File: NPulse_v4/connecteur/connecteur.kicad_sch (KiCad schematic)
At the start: 72 parts, among them J1 Conn_01x01, J10 Conn_02x05_Odd_Even, J11 Conn_01x01, J12 Conn_01x01, J13 Conn_02x05_Odd_Even, J14 Conn_01x01, J15 Conn_01x01, J16 Conn_01x01, J17 Conn_01x01, J18 Conn_01x01, J19 Conn_01x01, J2 Conn_01x01, J20 Conn_01x01, J21 Conn_01x01, J22 Conn_01x01, J23 Conn_01x01, J25 Conn_01x01, J26 Conn_01x01, J27 Conn_01x01, J29 Conn_01x01, J3 Conn_01x01, J30 Conn_01x01, J32 Conn_02x05_Odd_Even, J34 Conn_01x01, J35 Conn_02x05_Odd_Even, J36 Conn_01x01, J37 Conn_01x01, J38 Conn_01x01, J39 Conn_01x01, J4 Conn_01x01, J40 Conn_01x01, J41 Conn_01x01, J42 Conn_01x01, J43 Conn_01x01, J44 Conn_01x01, J45 Conn_01x01, J46 Conn_01x01, J47 Conn_01x01, J48 Conn_01x01, J49 Conn_01x01, J5 Conn_01x01, J50 Conn_01x01, J51 Conn_01x01, J52 Conn_01x01, J53 Conn_01x01, J54 Conn_02x05_Odd_Even, J55 Conn_01x01, J56 Conn_01x01, J57 Conn_02x05_Odd_Even, J58 Conn_01x01, J59 Conn_01x01, J6 Conn_01x01, J60 Conn_01x01, J61 Conn_01x01, J62 Conn_01x01, J63 Conn_01x01, J64 Conn_01x01, J65 Conn_01x01, J66 Conn_01x01, J67 Conn_01x01, J68 Conn_01x01, J69 Conn_01x01, J7 Conn_01x01, J70 Conn_01x01, J71 Conn_01x01, J72 Conn_01x01, J73 Conn_01x01, J74 Conn_01x01, J75 Conn_01x01, J76 Conn_01x01, J8 Conn_01x01, J9 Conn_01x01

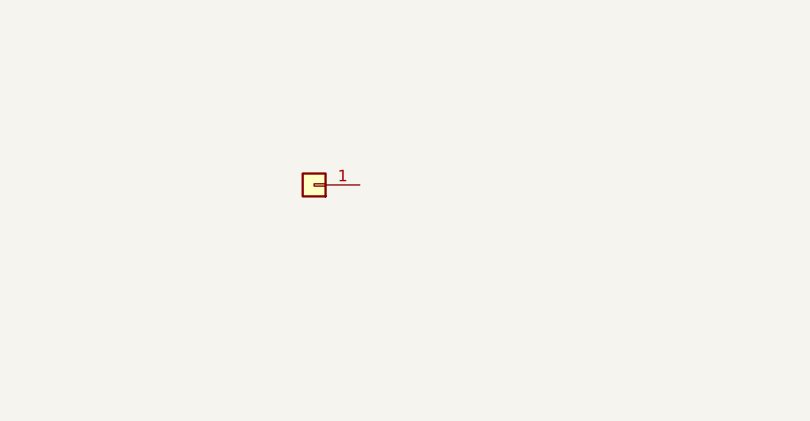
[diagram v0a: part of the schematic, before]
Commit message: Udate mounting holes positions
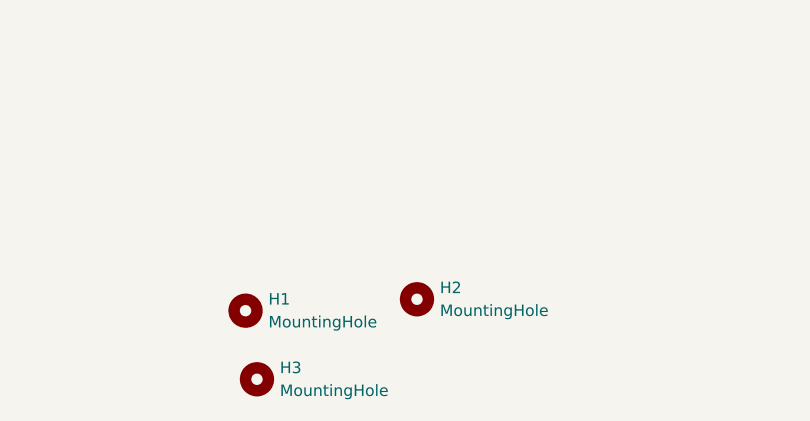
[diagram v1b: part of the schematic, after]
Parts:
- removed J71: Conn_01x01, Connector_Wire:SolderWire-0.1sqmm_1x01_D0.4mm_OD1mm, symbol Connector_Generic:Conn_01x01
- added H1, H2, H3: MountingHole, MountingHole:MountingHole_2.2mm_M2, symbol Mechanical:MountingHole
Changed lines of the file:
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@@
 (kicad_sch
-	(version 20231120)
+	(version 20250114)
 	(generator "eeschema")
-	(generator_version "8.0")
+	(generator_version "9.0")
 	(paper "A4")
 	(junction
@@
 	(label "+12V"
 		(at 179.07 72.39 90)
-		(fields_autoplaced yes)
 		(effects
 			(font
@@
 	(label "GND"
 		(at 207.01 50.8 90)
-		(fields_autoplaced yes)
 		(effects
 			(font
@@
 	(label "SCK_CON"
 		(at 181.61 50.8 90)
-		(fields_autoplaced yes)
 		(effects
 			(font
@@
 	(label "+12V"
 		(at 179.07 50.8 90)
-		(fields_autoplaced yes)
 		(effects
 			(font
@@
 	(label "MOSI_CON"
 		(at 184.15 50.8 90)
-		(fields_autoplaced yes)
 		(effects
 			(font
@@
 	(label "GND"
 		(at 204.47 50.8 90)
-		(fields_autoplaced yes)
 		(effects
 			(font
@@
 	(label "GND"
 		(at 196.85 50.8 90)
-		(fields_autoplaced yes)
 		(effects
 			(font
@@
 	(label "+5V"
 		(at 173.99 50.8 90)
-		(fields_autoplaced yes)
 		(effects
 			(font
@@
 	(label "+12V"
 		(at 176.53 72.39 90)
-		(fields_autoplaced yes)
 		(effects
 			(font
@@
 	(label "+12V"
 		(at 176.53 50.8 90)
-		(fields_autoplaced yes)
 		(effects
 			(font
@@
 	(label "MISO_CON"
 		(at 184.15 72.39 90)
-		(fields_autoplaced yes)
 		(effects
 			(font
@@
 	(label "NSS_CON"
 		(at 181.61 72.39 90)
-		(fields_autoplaced yes)
 		(effects
 			(font
@@
 	(label "GND"
 		(at 201.93 50.8 90)
-		(fields_autoplaced yes)
 		(effects
 			(font
@@
 	(label "GND"
 		(at 199.39 50.8 90)
-		(fields_autoplaced yes)
 		(effects
 			(font
@@
 	)
 	(symbol
+		(lib_id "Mechanical:MountingHole")
+		(at 134.62 167.64 0)
+		(unit 1)
+		(exclude_from_sim yes)
+		(in_bom no)
+		(on_board yes)
+		(dnp no)
+		(fields_autoplaced yes)
+		(property "Reference" "H2"
+			(at 137.16 166.3699 0)
+			(effects
+				(font
+					(size 1.27 1.27)
+				)
+				(justify left)
+			)
+		)
+		(property "Value" "MountingHole"
+			(at 137.16 168.9099 0)
+			(effects
+				(font
+					(size 1.27 1.27)
+				)
+				(justify left)
+			)
+		)
+		(property "Footprint" "MountingHole:MountingHole_2.2mm_M2"
+			(at 134.62 167.64 0)
+			(effects
+				(font
+					(size 1.27 1.27)
+				)
+				(hide yes)
+			)
+		)
+		(property "Datasheet" "~"
+			(at 134.62 167.64 0)
+			(effects
+				(font
+					(size 1.27 1.27)
+				)
+				(hide yes)
+			)
+		)
+		(property "Description" "Mounting Hole without connection"
+			(at 134.62 167.64 0)
+			(effects
+				(font
+					(size 1.27 1.27)
+				)
+				(hide yes)
+			)
+		)
+		(instances
+			(project "connecteur"
+				(path "/d1d459bc-21c9-4561-bf30-d30bab78c009"
+					(reference "H2")
+					(unit 1)
+				)
+			)
+		)
+	)
+	(symbol
 		(lib_id "power:+5V")
 		(at 196.85 96.52 0)
@@
 	)
 	(symbol
+		(lib_id "Mechanical:MountingHole")
+		(at 116.84 176.53 0)
+		(unit 1)
+		(exclude_from_sim yes)
+		(in_bom no)
+		(on_board yes)
+		(dnp no)
+		(fields_autoplaced yes)
+		(property "Reference" "H3"
+			(at 119.38 175.2599 0)
+			(effects
+				(font
+					(size 1.27 1.27)
+				)
+				(justify left)
+			)
+		)
+		(property "Value" "MountingHole"
+			(at 119.38 177.7999 0)
+			(effects
+				(font
+					(size 1.27 1.27)
+				)
+				(justify left)
+			)
+		)
+		(property "Footprint" "MountingHole:MountingHole_2.2mm_M2"
+			(at 116.84 176.53 0)
+			(effects
+				(font
+					(size 1.27 1.27)
+				)
+				(hide yes)
+			)
+		)
+		(property "Datasheet" "~"
+			(at 116.84 176.53 0)
+			(effects
+				(font
+					(size 1.27 1.27)
+				)
+				(hide yes)
+			)
+		)
+		(property "Description" "Mounting Hole without connection"
+			(at 116.84 176.53 0)
+			(effects
+				(font
+					(size 1.27 1.27)
+				)
+				(hide yes)
+			)
+		)
+		(instances
+			(project "connecteur"
+				(path "/d1d459bc-21c9-4561-bf30-d30bab78c009"
+					(reference "H3")
+					(unit 1)
+				)
+			)
+		)
+	)
+	(symbol
 		(lib_id "power:+5V")
 		(at 115.57 116.84 270)
@@
 	)
 	(symbol
+		(lib_id "Mechanical:MountingHole")
+		(at 115.57 168.91 0)
+		(unit 1)
+		(exclude_from_sim yes)
+		(in_bom no)
+		(on_board yes)
+		(dnp no)
+		(fields_autoplaced yes)
+		(property "Reference" "H1"
+			(at 118.11 167.6399 0)
+			(effects
+				(font
+					(size 1.27 1.27)
+				)
+				(justify left)
+			)
+		)
+		(property "Value" "MountingHole"
+			(at 118.11 170.1799 0)
+			(effects
+				(font
+					(size 1.27 1.27)
+				)
+				(justify left)
+			)
+		)
+		(property "Footprint" "MountingHole:MountingHole_2.2mm_M2"
+			(at 115.57 168.91 0)
+			(effects
+				(font
+					(size 1.27 1.27)
+				)
+				(hide yes)
+			)
+		)
+		(property "Datasheet" "~"
+			(at 115.57 168.91 0)
+			(effects
+				(font
+					(size 1.27 1.27)
+				)
+				(hide yes)
+			)
+		)
+		(property "Description" "Mounting Hole without connection"
+			(at 115.57 168.91 0)
+			(effects
+				(font
+					(size 1.27 1.27)
+				)
+				(hide yes)
+			)
+		)
+		(instances
+			(project ""
+				(path "/d1d459bc-21c9-4561-bf30-d30bab78c009"
+					(reference "H1")
+					(unit 1)
+				)
+			)
+		)
+	)
+	(symbol
 		(lib_id "Connector_Generic:Conn_01x01")
 		(at 242.57 73.66 0)
@@
 	(symbol
 		(lib_id "Connector_Generic:Conn_01x01")
-		(at 123.19 154.94 180)
-		(unit 1)
-		(exclude_from_sim no)
-		(in_bom yes)
-		(on_board yes)
-		(dnp no)
-		(fields_autoplaced yes)
-		(property "Reference" "J71"
-			(at 123.19 148.59 0)
-			(effects
-				(font
-					(size 1.27 1.27)
-				)
-				(hide yes)
-			)
-		)
-		(property "Value" "Conn_01x01"
-			(at 123.19 151.13 0)
-			(effects
-				(font
-					(size 1.27 1.27)
-				)
-				(hide yes)
-			)
-		)
-		(property "Footprint" "Connector_Wire:SolderWire-0.1sqmm_1x01_D0.4mm_OD1mm"
-			(at 123.19 154.94 0)
-			(effects
-				(font
-					(size 1.27 1.27)
-				)
-				(hide yes)
-			)
-		)
-		(property "Datasheet" "~"
-			(at 123.19 154.94 0)
-			(effects
-				(font
-					(size 1.27 1.27)
-				)
-				(hide yes)
-			)
-		)
-		(property "Description" "Generic connector, single row, 01x01, script generated (kicad-library-utils/schlib/autogen/connector/)"
-			(at 123.19 154.94 0)
-			(effects
-				(font
-					(size 1.27 1.27)
-				)
-				(hide yes)
-			)
-		)
-		(pin "1"
-		)
-		(instances
-			(project "connecteur"
-				(path "/d1d459bc-21c9-4561-bf30-d30bab78c009"
-					(reference "J71")
-					(unit 1)
-				)
-			)
-		)
-	)
-	(symbol
-		(lib_id "Connector_Generic:Conn_01x01")
 		(at 181.61 82.55 270)
 		(unit 1)
@@
 		)
 	)
+	(embedded_fonts no)
 )

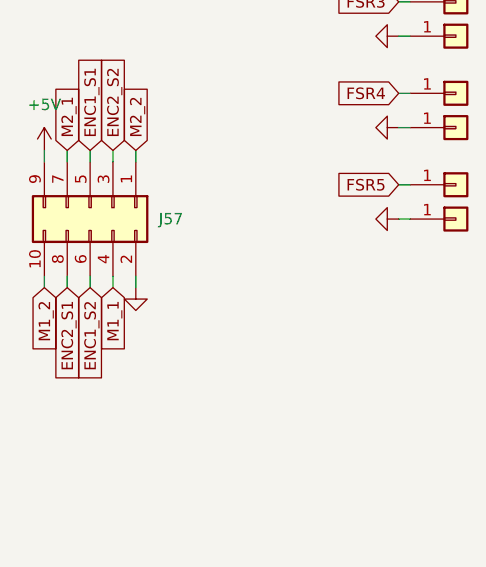
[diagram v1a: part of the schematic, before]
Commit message: add 5v-gnd pair
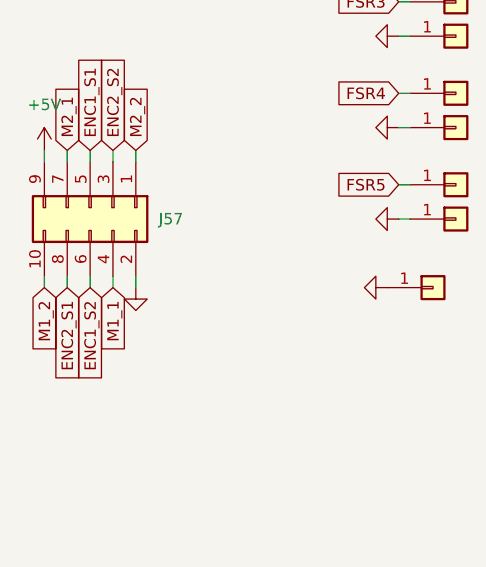
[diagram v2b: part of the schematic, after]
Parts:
- added J77: Conn_01x01, Connector_Wire:SolderWire-0.1sqmm_1x01_D0.4mm_OD1mm, symbol Connector_Generic:Conn_01x01
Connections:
- net GND: now also J77.1 (Pin_1)
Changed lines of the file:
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@@
+	(symbol
+		(lib_id "Connector_Generic:Conn_01x01")
+		(at 240.03 111.76 0)
+		(unit 1)
+		(exclude_from_sim no)
+		(in_bom yes)
+		(on_board yes)
+		(dnp no)
+		(fields_autoplaced yes)
+		(property "Reference" "J77"
+			(at 241.3001 114.3 90)
+			(effects
+				(font
+					(size 1.27 1.27)
+				)
+				(justify right)
+				(hide yes)
+			)
+		)
+		(property "Value" "Conn_01x01"
+			(at 238.7601 114.3 90)
+			(effects
+				(font
+					(size 1.27 1.27)
+				)
+				(justify right)
+				(hide yes)
+			)
+		)
+		(property "Footprint" "Connector_Wire:SolderWire-0.1sqmm_1x01_D0.4mm_OD1mm"
+			(at 240.03 111.76 0)
+			(effects
+				(font
+					(size 1.27 1.27)
+				)
+				(hide yes)
+			)
+		)
+		(property "Datasheet" "~"
+			(at 240.03 111.76 0)
+			(effects
+				(font
+					(size 1.27 1.27)
+				)
+				(hide yes)
+			)
+		)
+		(property "Description" "Generic connector, single row, 01x01, script generated (kicad-library-utils/schlib/autogen/connector/)"
+			(at 240.03 111.76 0)
+			(effects
+				(font
+					(size 1.27 1.27)
+				)
+				(hide yes)
+			)
+		)
+		(pin "1"
+		)
+		(instances
+			(project "connecteur"
+				(path "/d1d459bc-21c9-4561-bf30-d30bab78c009"
+					(reference "J77")
+					(unit 1)
+				)
+			)
+		)
+	)
 	(symbol
 		(lib_id "Connector_Generic:Conn_01x01")
@@
 					(unit 1)
 				)
+			)
+		)
+	)
+	(symbol
+		(lib_id "power:GND")
+		(at 234.95 111.76 270)
+		(unit 1)
+		(exclude_from_sim no)
+		(in_bom yes)
+		(on_board yes)
+		(dnp no)
+		(fields_autoplaced yes)
+		(property "Reference" "#PWR030"
+			(at 228.6 111.76 0)
+			(effects
+				(font
+					(size 1.27 1.27)
+				)
+				(hide yes)
+			)
+		)
+		(property "Value" "GND"
+			(at 231.14 111.7601 90)
+			(effects
+				(font
+					(size 1.27 1.27)
+				)
+				(justify right)
+				(hide yes)
+			)
+		)
+		(property "Footprint" ""
+			(at 234.95 111.76 0)
+			(effects
+				(font
+					(size 1.27 1.27)
+				)
+				(hide yes)
+			)
+		)
+		(property "Datasheet" ""
+			(at 234.95 111.76 0)
+			(effects
+				(font
+					(size 1.27 1.27)
+				)
+				(hide yes)
+			)
+		)
+		(property "Description" "Power symbol creates a global label with name \"GND\" , ground"
+			(at 234.95 111.76 0)
+			(effects
+				(font
+					(size 1.27 1.27)
+				)
+				(hide yes)
+			)
+		)
+		(pin "1"
+		)
+		(instances
+			(project "connecteur"
+				(path "/d1d459bc-21c9-4561-bf30-d30bab78c009"
+					(reference "#PWR030")
+					(unit 1)
+				)
